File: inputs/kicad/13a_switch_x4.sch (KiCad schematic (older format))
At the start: 6 parts, among them P1 MOLEX-0431603103, P2 MOLEX-0431603103

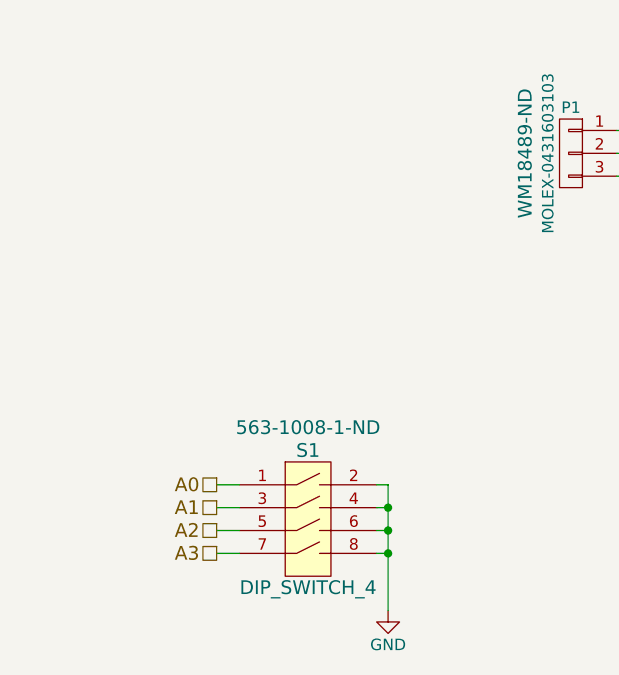
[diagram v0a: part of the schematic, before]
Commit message: [inputs] Updating to use standard libraries
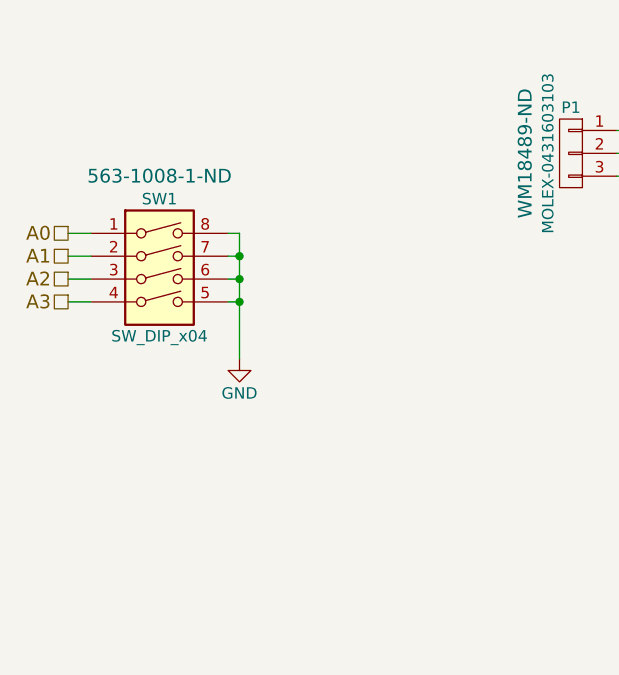
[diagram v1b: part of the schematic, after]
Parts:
- removed S1: DIP_SWITCH_4, footprints:Copal_CHS-04TB, symbol DIP_SWITCH_4
- added SW1: SW_DIP_x04, Buttons_Switches_SMD:SW_DIP_x4_W7.62mm_Slide_Copal_CHS-B, symbol SW_DIP_x04
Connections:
- net A0: now also SW1.1
- net A1: now also SW1.2
- net A2: now also SW1.3
- net A3: now also SW1.4
- net GND: now also SW1.5, SW1.6, SW1.7, SW1.8
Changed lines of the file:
@@
 EESchema Schematic File Version 2
+LIBS:microchip_pic16mcu
 LIBS:power
 LIBS:device
@@
 LIBS:valves
 LIBS:inputs
-LIBS:fluffy-potato
+LIBS:switches
+LIBS:rfcom
 LIBS:inputs-cache
 EELAYER 25 0
@@
 L GND #PWR08
 U 1 1 584497B3
-P 4050 5200
-F 0 "#PWR08" H 4050 4950 50  0001 C CNN
-F 1 "GND" H 4050 5050 50  0000 C CNN
-F 2 "" H 4050 5200 50  0000 C CNN
-F 3 "" H 4050 5200 50  0000 C CNN
-	1    4050 5200
-	1    0    0    -1
-$EndComp
-Wire Wire Line
-	4050 4950 4000 4950
-Wire Wire Line
-	4050 4650 4050 5200
-Wire Wire Line
-	4000 4850 4050 4850
-Connection ~ 4050 4950
-Wire Wire Line
-	4000 4750 4050 4750
-Connection ~ 4050 4850
-Wire Wire Line
-	4000 4650 4050 4650
-Connection ~ 4050 4750
-$Comp
-L DIP_SWITCH_4 S1
-U 1 1 5844A01A
-P 3700 4800
-F 0 "S1" H 3700 5100 60  0000 C CNN
-F 1 "DIP_SWITCH_4" H 3700 4500 60  0000 C CNN
-F 2 "footprints:Copal_CHS-04TB" H 3750 5150 60  0001 C CNN
-F 3 "http://www.nidec-copal-electronics.com/e/catalog/switch/chs.pdf" H 3750 5150 60  0001 C CNN
-F 4 "563-1008-1-ND" H 3700 5200 60  0000 C CNN "DIGIKEY"
-	1    3700 4800
-	1    0    0    -1
-$EndComp
-Wire Wire Line
-	3300 4950 3400 4950
-Wire Wire Line
-	3300 4850 3400 4850
-Wire Wire Line
-	3300 4750 3400 4750
-Wire Wire Line
-	3300 4650 3400 4650
+P 3400 4100
+F 0 "#PWR08" H 3400 3850 50  0001 C CNN
+F 1 "GND" H 3400 3950 50  0000 C CNN
+F 2 "" H 3400 4100 50  0000 C CNN
+F 3 "" H 3400 4100 50  0000 C CNN
+	1    3400 4100
+	1    0    0    -1
+$EndComp
+Wire Wire Line
+	3400 3850 3350 3850
+Wire Wire Line
+	3400 3550 3400 4100
+Wire Wire Line
+	3350 3750 3400 3750
+Connection ~ 3400 3850
+Wire Wire Line
+	3350 3650 3400 3650
+Connection ~ 3400 3750
+Wire Wire Line
+	3350 3550 3400 3550
+Connection ~ 3400 3650
+Wire Wire Line
+	2650 3850 2750 3850
+Wire Wire Line
+	2650 3750 2750 3750
+Wire Wire Line
+	2650 3650 2750 3650
+Wire Wire Line
+	2650 3550 2750 3550
 Wire Wire Line
 	6450 2650 6450 2750
@@
 Wire Wire Line
 	5750 4850 5750 4700
-Text HLabel 3300 4650 0    60   UnSpc ~ 0
+Text HLabel 2650 3550 0    60   UnSpc ~ 0
 A0
-Text HLabel 3300 4750 0    60   UnSpc ~ 0
+Text HLabel 2650 3650 0    60   UnSpc ~ 0
 A1
-Text HLabel 3300 4850 0    60   UnSpc ~ 0
+Text HLabel 2650 3750 0    60   UnSpc ~ 0
 A2
-Text HLabel 3300 4950 0    60   UnSpc ~ 0
+Text HLabel 2650 3850 0    60   UnSpc ~ 0
 A3
 Wire Wire Line
@@
 	7900 3650 7900 3400
 Connection ~ 6400 3300
+$Comp
+L SW_DIP_x04 SW1
+U 1 1 5862F22E
+P 3050 3750
+F 0 "SW1" H 3050 4100 50  0000 C CNN
+F 1 "SW_DIP_x04" H 3050 3500 50  0000 C CNN
+F 2 "Buttons_Switches_SMD:SW_DIP_x4_W7.62mm_Slide_Copal_CHS-B" H 3050 3750 50  0001 C CNN
+F 3 "" H 3050 3750 50  0000 C CNN
+F 4 "563-1008-1-ND" H 3050 4200 60  0000 C CNN "DIGIKEY"
+	1    3050 3750
+	1    0    0    -1
+$EndComp
 $EndSCHEMATC
